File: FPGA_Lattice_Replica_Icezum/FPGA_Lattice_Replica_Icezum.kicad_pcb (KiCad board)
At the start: 4 copper layers, 86.5 x 62.1 mm, 161 parts, among them J1 USB_Micro_Type_B, J11 1x6_female_pin_Header_2.54mm, J13 1x6_female_pin_Header_2.54mm, J14 1x6_female_pin_Header_2.54mm, J18 Power_Jack, J19 2x4_male_pin_Header_2.54mm, J5 1x8_male_pin_Header_2.54mm, Q1 DMP3017, Q2 DMP3017, Q3 DMP2035U-7, Q4 Mosfet_P_DFN-6, Q5 PMBT3906, SW1 SW1, SW2 Switch_4p, SW3 SPDT_Switch, SW4 Switch, U1 iCE40HX1K-TQ144, U10 AP7361, U11 TLV711, U12 TPS62133RGTR, U13 APX810, U2 N25Q032A, U3 FT2232H, U4 DSC1001, U5 93LC56C, U8 TXB0108

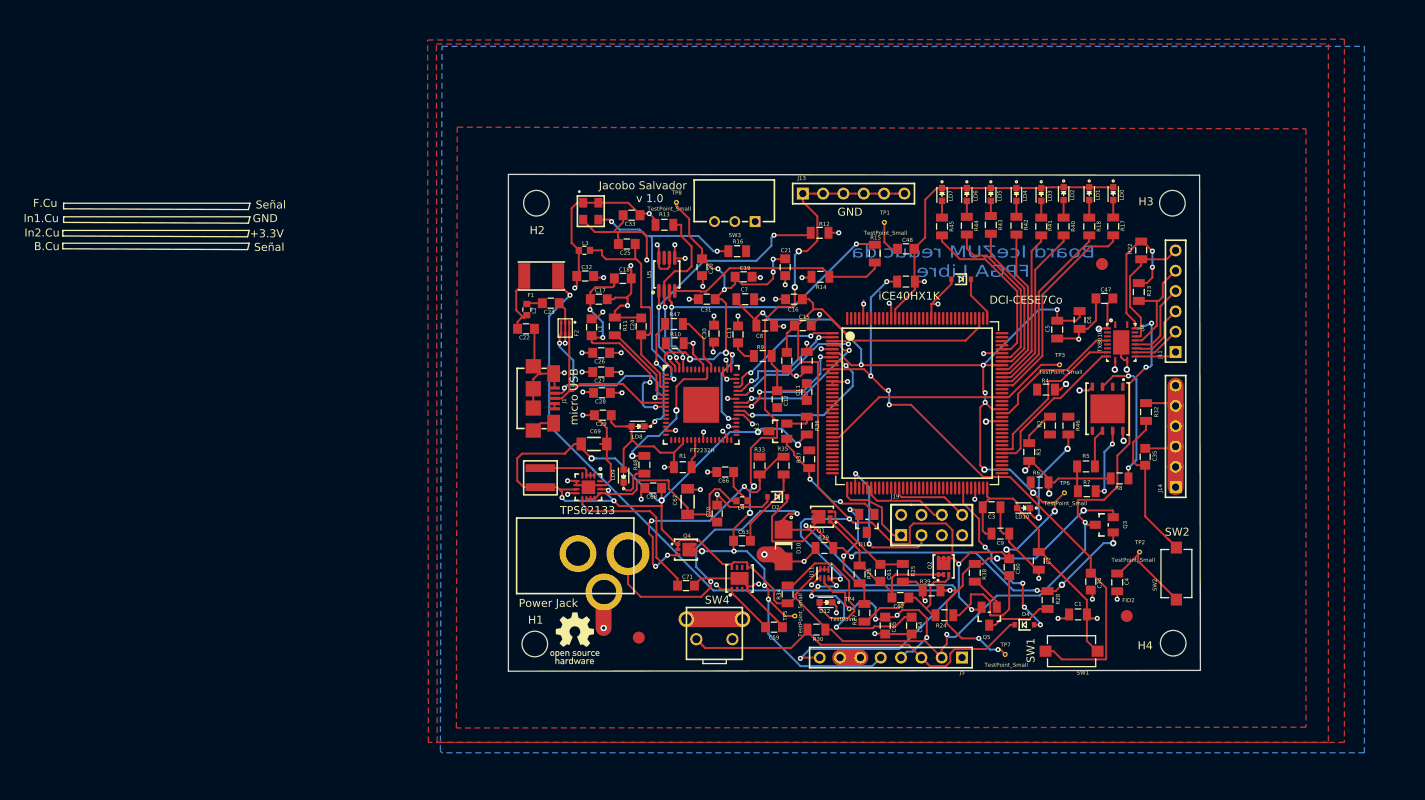
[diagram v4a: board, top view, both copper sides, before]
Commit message: correcciones de serigrafia, componentes 3D, se corrigio relleno de cobre, simetria en agujero y cambio en la grilla para corte de placa, se corrigieron cuestion de ruteo y uniformidad en la vias. Se agrego mas especificaciones para el fabricante
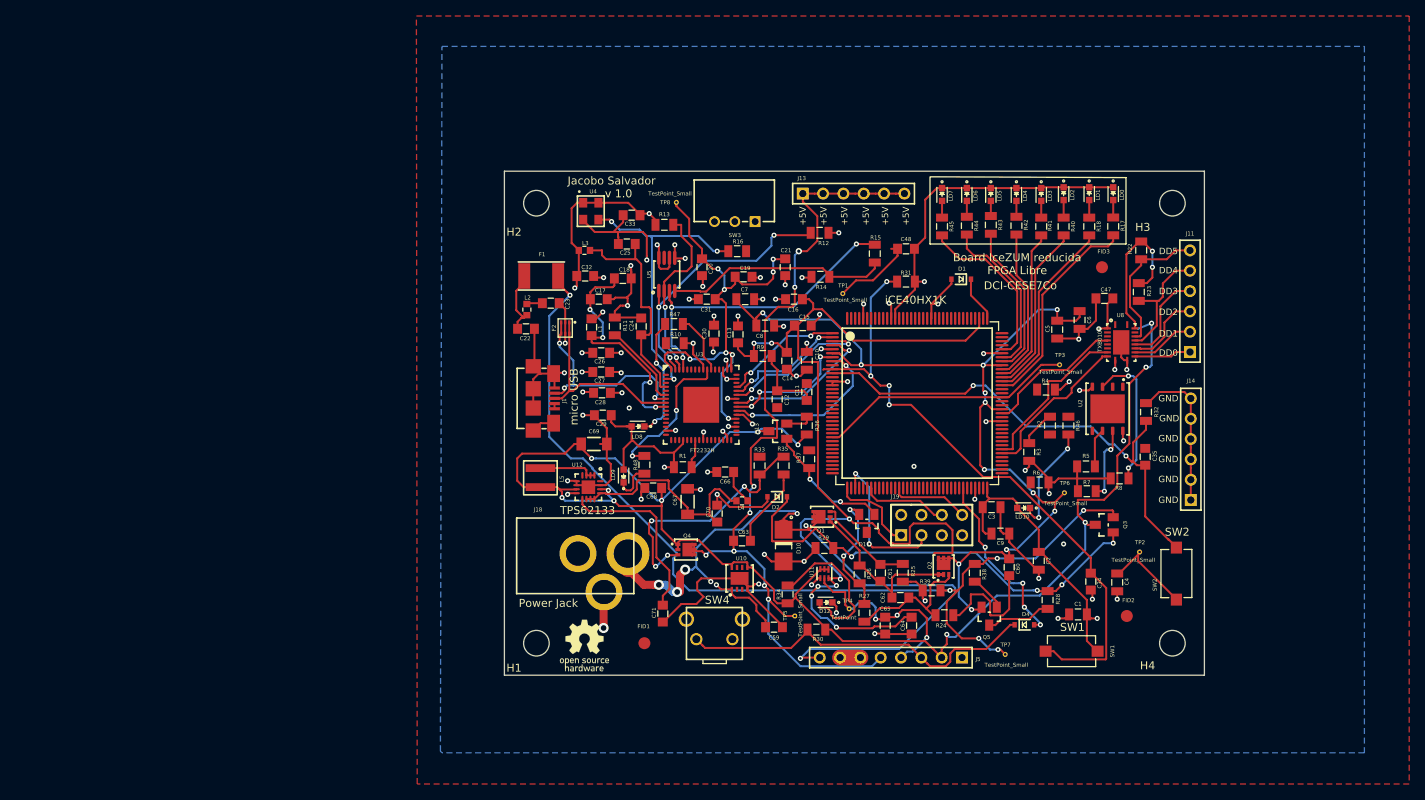
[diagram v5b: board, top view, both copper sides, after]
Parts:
- H1, H2, H3, H4: value MountingHole -> MH
- moved TP1 10.3 mm to (150.8, 76.8)
- moved C71 4.55 mm to (128.3, 116.8), turned to 270 degrees
- moved J14 2.48 mm to (194.3, 102.6)
- moved J11 1.80 mm to (194.2, 84.1)
- moved G*** 1.50 mm to (118.5, 120.8)
- moved FID1 0.99 mm to (126.0, 120.5)
- moved FID3 0.40 mm to (183.2, 73.5)
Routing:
- net U_SW2: track 19.4 -> 62.4 mm, vias 0 -> 2
- net (no net): track 7.01 -> 0.00 mm
- net GND: track 266.9 -> 273.7 mm, vias 56 -> 59
- net +5V: track 218.1 -> 224.2 mm
- net +1V2: track 158.1 -> 162.5 mm, vias 6 -> 8
- net USB_5V: track 121.1 -> 124.3 mm
- net Net-(C71-Pad1): track 20.2 -> 22.6 mm
- net VIN: track 95.3 -> 93.2 mm, vias 4 -> 7
- net /socketsAndHeaders/DD5: track 16.2 -> 18.0 mm
- net /socketsAndHeaders/DD4: track 13.7 -> 15.5 mm
- net /socketsAndHeaders/DD3: track 10.0 -> 11.8 mm
- net /socketsAndHeaders/DD2: track 8.08 -> 9.88 mm
- net /socketsAndHeaders/DD1: track 6.16 -> 7.96 mm
- net /socketsAndHeaders/DD0: track 5.31 -> 7.11 mm
- net +5V_P: track 106.7 -> 107.9 mm
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- added copper zone on F.Cu, net GND
- removed copper zone on F.Cu, net (none)
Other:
- board size 86.5 x 62.1 mm -> 87.5 x 63 mm
- rule via_min_size: 0.4 -> 0.64
- board text added: "+5V"
- board text added: "DD0"
- board text added: "DD1"
- board text added: "DD2"
- board text added: "DD3"
- board text added: "DD4"
- board text added: "DD5"
- board text added: "Nota para fabricante Terminación HASL"
- board text added: "Notas: modelo de 4 capas capas externas: señales capas internas: In1.Cu: GND In2.Cu:+3.3V ----------------------- Grilla: 0.1 mm Ancho de pista: 0.25 mm y 1 mm vías 0.64 / 0.3 mm vias 1.27 / 0.70 mm para alimentación ----------------------- Superfie rectangular 87.5 x 63.0 mm Línea de corte realizada con grilla de 0,5 mm"
- board text added: "Stackup F.Cu: señal In1.Cu: GND In2.Cu: Vcc B.Cu: señal"
- board text removed: "+3.3V"
- board text removed: "B.Cu"
- board text removed: "F.Cu"
- board text removed: "In1.Cu"
- board text removed: "In2.Cu"
- board text removed: "Nota para fabricante Terminación HALS"
- board text removed: "Notas: modelo de 4 capas capas externas: señales capas internas: In1.Cu: GND In2.Cu:+3.3V ------------- Grilla: 0.1 mm Ancho de pista: 0.254 mm vías 0.64 / 0.3 mm ------------- Superfie rectangular 86.4 x 61.9 mm"
- board text removed: "Señal"
- board text removed: "Stackup"
- board text removed: "https://github.com/FPGAwars/icezum.git"
